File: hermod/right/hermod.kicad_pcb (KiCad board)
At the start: 2 copper layers, 154 x 149.2 mm, 164 parts, among them J1 USB_C_Receptacle_USB2.0, J2 Conn_01x05, J3 USB_C_Receptacle_USB2.0, Q1 AO3401A, Q2 MMUN2233LT1G, U1 STM32F072CBT6, U2 PRTR5V0U2X, U3 XC6206PxxxMR-Regulator_Linear, U4 CR2013-MI2120, U5 TXB0101

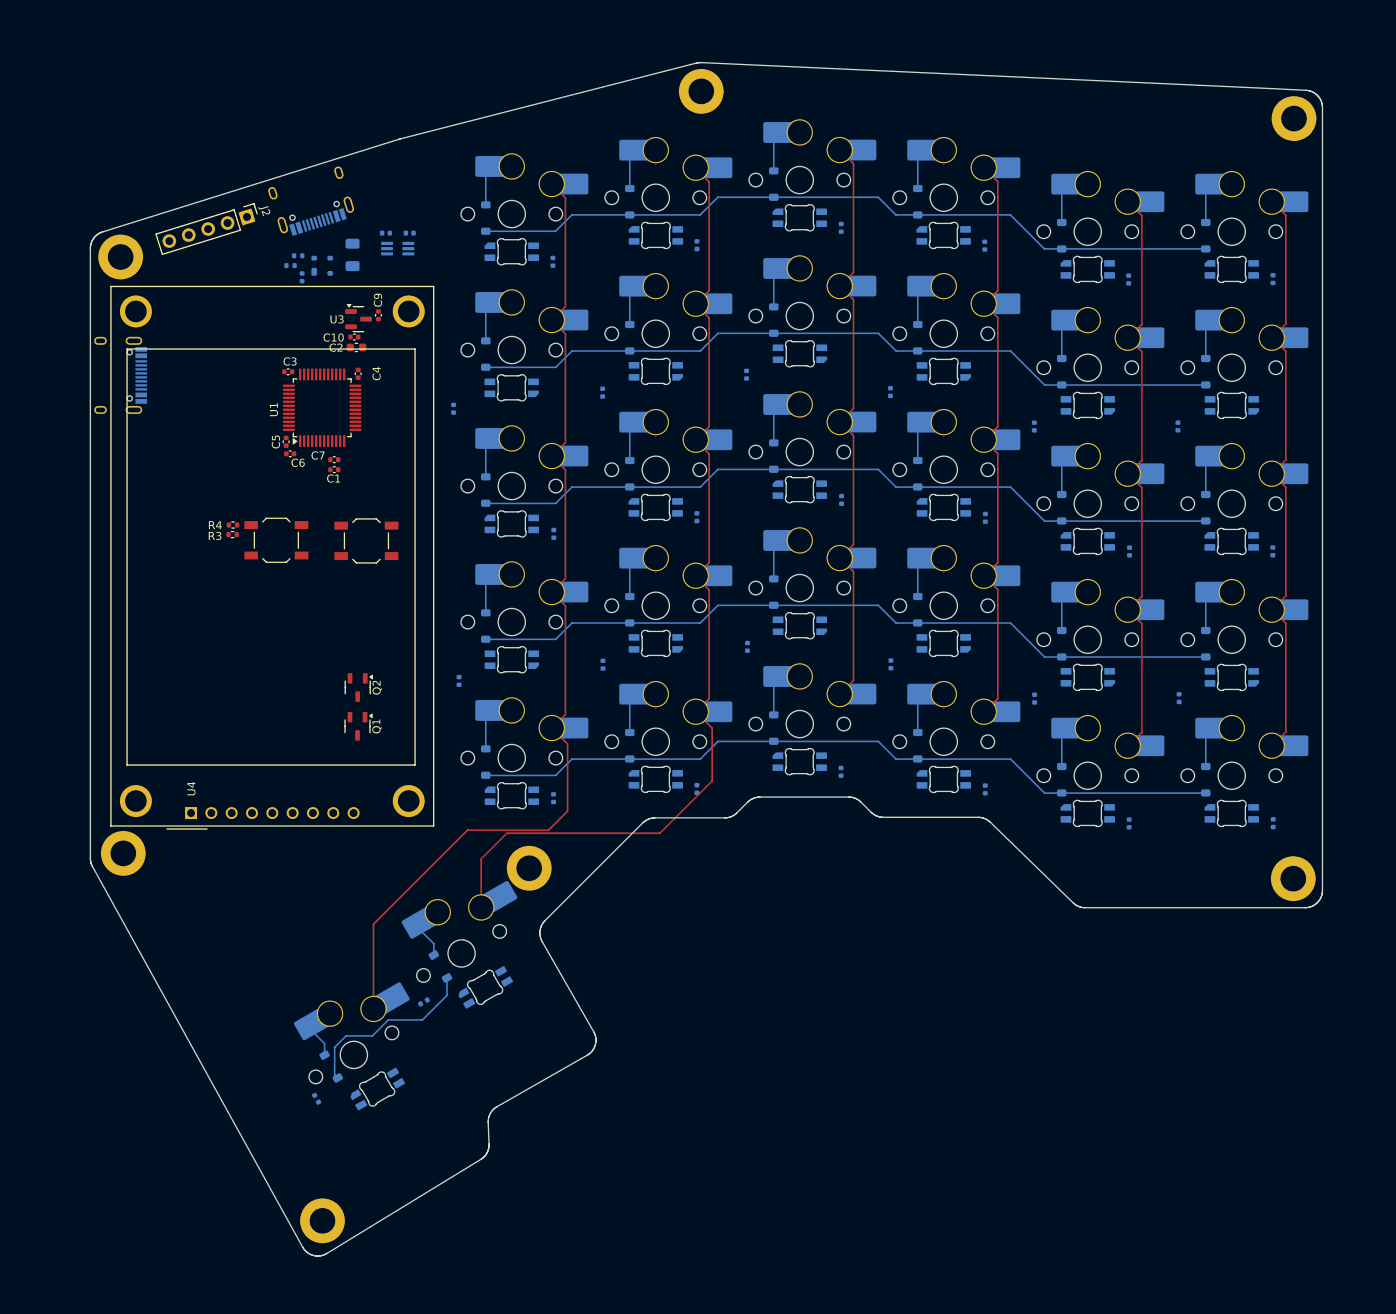
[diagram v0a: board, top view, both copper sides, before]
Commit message: Wired the LEDs on the right
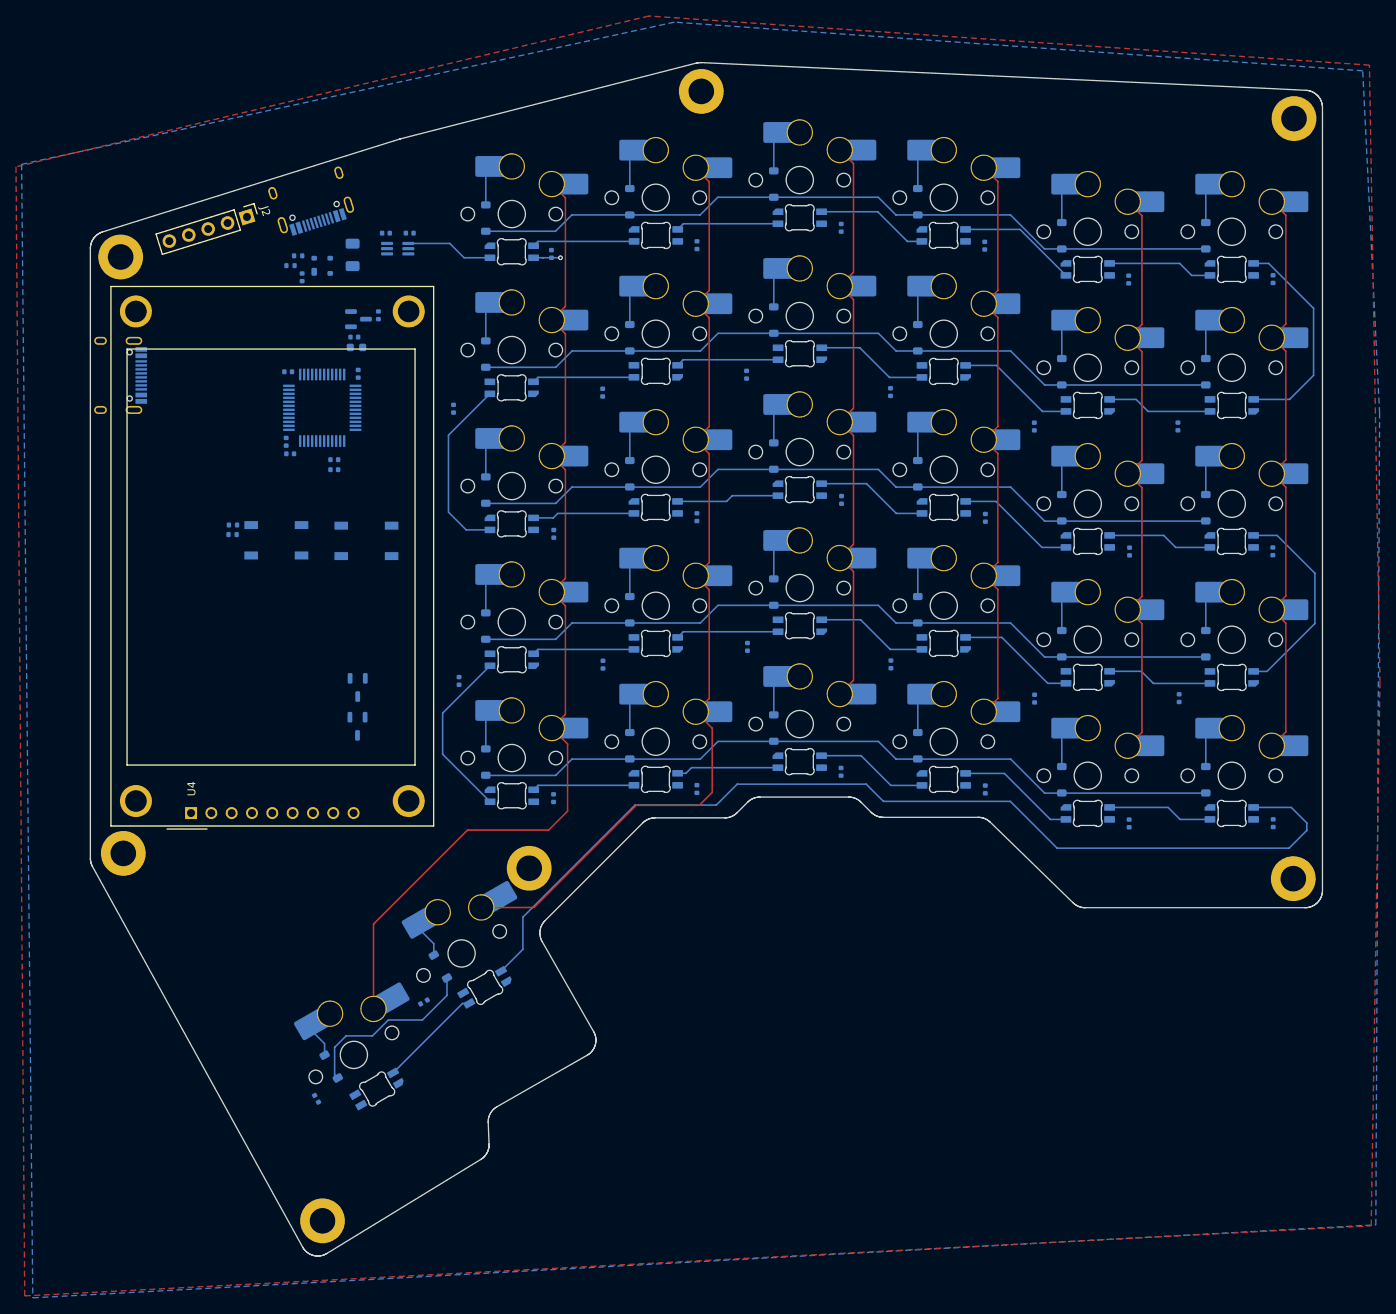
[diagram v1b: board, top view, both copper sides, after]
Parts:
- BOOT1, C1, C10, C2, C3, C4, C5, C6, C7, C9, Q1, Q2, R3, R4, RST1, U1, U3: moved to B.Cu
- moved C11 1.00 mm to (88.4, 42.2), turned to 90 degrees
- turned BOOT1 to 0 degrees
- turned C7 to 0 degrees
- turned LED31 to 30 degrees
- turned LED32 to 30 degrees
- turned RST1 to 180 degrees
- turned U5 to 0 degrees
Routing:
- net DOut5: track 0.00 -> 125.4 mm
- net DOut1: track 0.00 -> 26.9 mm
- net DOut3: track 0.00 -> 26.1 mm
- net DOut2: track 0.00 -> 23.0 mm
- net DOut4: track 0.00 -> 21.9 mm
- net Net-(LED4-DOUT): track 0.00 -> 14.9 mm
- net Net-(LED20-DOUT): track 0.00 -> 14.9 mm
- net Net-(LED8-DOUT): track 0.00 -> 14.9 mm
- net Net-(LED28-DOUT): track 0.00 -> 14.9 mm
- net Net-(LED16-DOUT): track 0.00 -> 14.9 mm
- net Net-(LED27-DOUT): track 0.00 -> 14.1 mm
- net Net-(LED15-DOUT): track 0.00 -> 14.1 mm
- net Net-(LED3-DOUT): track 0.00 -> 14.1 mm
- net Net-(LED10-DIN): track 0.00 -> 14.1 mm
- net Net-(LED21-DOUT): track 0.00 -> 14.1 mm
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- added copper zone on F.Cu, net +5V
- added copper zone on B.Cu, net GND

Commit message: Wired up rows and cols
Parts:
- turned U1 to -90 degrees
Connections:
- U1 pad 12: row5 -> row0
- U1 pad 13: col1 -> col0
- U1 pad 14: col2 -> col1
- U1 pad 15: col3 -> col2
- U1 pad 16: col4 -> col3
- U1 pad 17: col5 -> col4
- U1 pad 18: row4 -> col5
- U1 pad 19: row3 -> row1
- U1 pad 21: row1 -> row3
- U1 pad 22: row0 -> row4
- U1 pad 25: col0 -> row5
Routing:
- net col0: track 73.6 -> 206.2 mm
- net col1: track 73.6 -> 187.9 mm
- net col2: track 73.6 -> 168.0 mm
- net row5: track 22.9 -> 108.6 mm
- net col3: track 73.6 -> 149.0 mm
- net row4: track 94.4 -> 151.2 mm
- net col4: track 119.4 -> 175.6 mm
- net row3: track 94.4 -> 134.7 mm
- net col5: track 125.5 -> 163.4 mm
- net row0: track 94.4 -> 124.5 mm
- net row2: track 94.4 -> 118.5 mm
- net row1: track 94.4 -> 112.9 mm
- net DOut4: track 21.9 -> 23.5 mm, vias 0 -> 2
- net DOut2: track 23.0 -> 22.8 mm, vias 0 -> 2
- net RGB5v: vias 0 -> 2

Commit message: Updated more wiring
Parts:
- moved F1 12.1 mm to (51.5, 44.1)
- moved C22 3.58 mm to (78.3, 58.6), turned to -90 degrees
- moved R1 1.81 mm to (57.0, 42.3)
- moved R2 1.37 mm to (55.8, 43.4)
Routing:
- net GND: track 0.00 -> 74.8 mm, vias 0 -> 1
- net D+: track 0.00 -> 32.1 mm, vias 0 -> 2
- net D-: track 0.00 -> 30.5 mm, vias 0 -> 2
- net RGB3.3: track 0.00 -> 29.4 mm, vias 0 -> 2
- net +3V3: track 0.00 -> 23.6 mm
- net VBUS: track 0.00 -> 23.0 mm
- net +5V: track 3.37 -> 17.6 mm, vias 1 -> 8
- net Net-(J1-CC2): track 0.00 -> 9.55 mm, vias 0 -> 2
- net Net-(J1-CC1): track 0.00 -> 4.36 mm
- net SplitSerial: track 0.00 -> 3.11 mm

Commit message: Finished wiring and addressed DRC
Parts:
- moved C6 11.5 mm to (55.7, 55.7)
- moved C4 8.46 mm to (64.2, 65.6), turned to -90 degrees
- moved C18 3.90 mm to (150.7, 60.4), turned to 180 degrees
- moved C30 3.83 mm to (150.6, 94.4), turned to 180 degrees
- moved C32 3.79 mm to (114.6, 87.9), turned to 180 degrees
- moved C17 3.79 mm to (168.5, 60.4), turned to 180 degrees
- moved C34 3.77 mm to (78.5, 92.2), turned to 180 degrees
- moved C33 3.76 mm to (96.6, 90.2), turned to 180 degrees
- moved C31 3.74 mm to (132.5, 90.2), turned to 180 degrees
- moved C21 3.66 mm to (96.2, 56.1), turned to 180 degrees
- moved C20 3.61 mm to (114.1, 53.9), turned to 180 degrees
- moved C19 3.59 mm to (132.3, 56.2), turned to 180 degrees
- moved C29 3.59 mm to (168.2, 94.4), turned to 180 degrees
- moved C41 3.04 mm to (75.4, 136.6), turned to -135 degrees
- moved C42 2.91 mm to (61.9, 148.5), turned to -150 degrees
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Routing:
- net +3V3: track 23.6 -> 177.0 mm, vias 0 -> 6
- net GND: track 74.8 -> 211.7 mm, vias 1 -> 89
- net +5V: track 17.6 -> 112.4 mm, vias 8 -> 38
- net LCD_CS: track 0.00 -> 60.5 mm, vias 0 -> 1
- net LCD_MOSI: track 0.00 -> 60.1 mm
- net LCD_RST: track 0.00 -> 58.9 mm
- net LCD_DC: track 0.00 -> 58.8 mm, vias 0 -> 1
- net NRST: track 0.00 -> 54.3 mm, vias 0 -> 3
- net LCD_MISO: track 0.00 -> 53.7 mm, vias 0 -> 2
- net LCD_SCK: track 0.00 -> 51.0 mm, vias 0 -> 2
- net SWCLK: track 0.00 -> 49.6 mm, vias 0 -> 1
- net LCD_PWR: track 0.00 -> 40.2 mm
- net LCD_EN: track 0.00 -> 38.7 mm, vias 0 -> 2
- net SWD: track 0.00 -> 32.3 mm, vias 0 -> 1
- net BOOT0: track 0.00 -> 27.7 mm, vias 0 -> 2
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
